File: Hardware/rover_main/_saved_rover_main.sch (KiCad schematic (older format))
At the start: 32 parts, among them J1 BATT, J10 Analog, J2 BME280, J3 CSS811, J4 DRIVERS, J5 GY-87, J6 PROG, J7 FTDI, J8 Digital, J9 i2c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

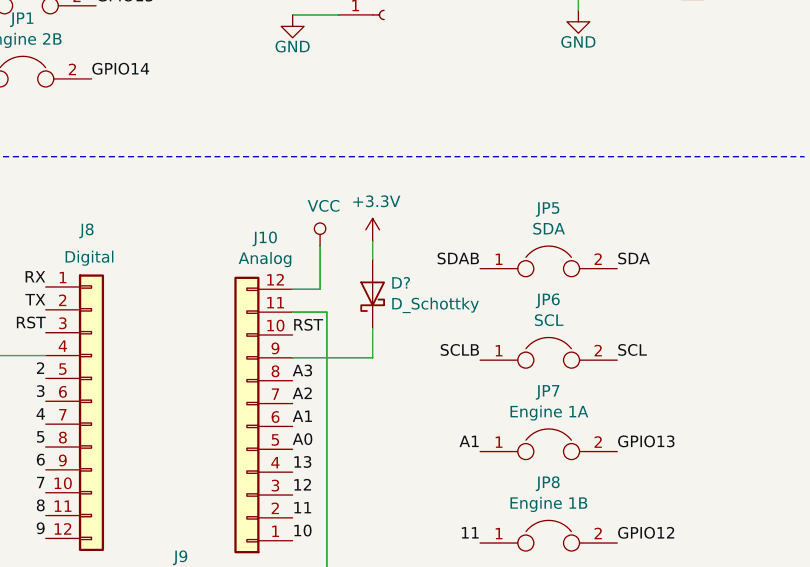
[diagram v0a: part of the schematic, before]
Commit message: ADD DIODE
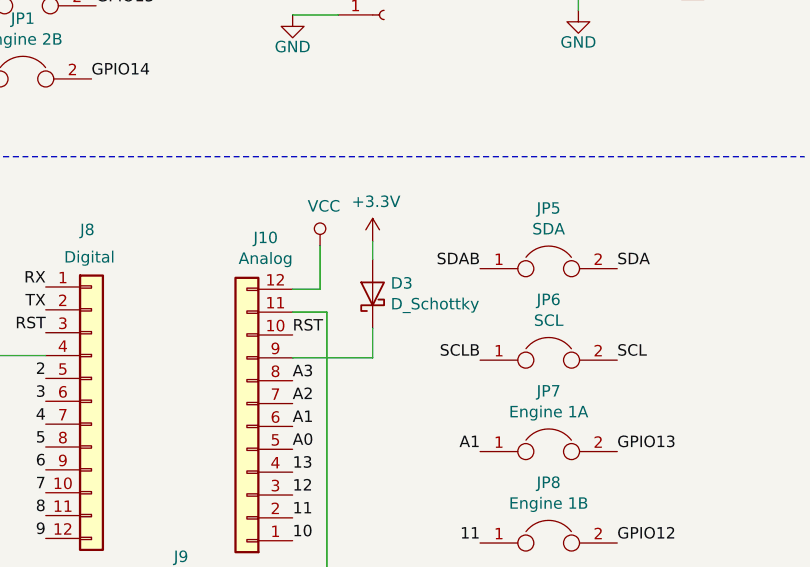
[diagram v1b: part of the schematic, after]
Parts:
- gave numbers to parts that had none: 1
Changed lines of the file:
@@
 NoConn ~ 2010 6710
 $Comp
-L Device:D_Schottky D?
+L Device:D_Schottky D3
 U 1 1 5D4CB997
 P 9330 4510
-F 0 "D?" V 9376 4431 50  0000 R CNN
+F 0 "D3" V 9376 4431 50  0000 R CNN
 F 1 "D_Schottky" V 9285 4431 50  0000 R CNN
 F 2 "Diode_THT:D_A-405_P10.16mm_Horizontal" H 9330 4510 50  0001 C CNN
